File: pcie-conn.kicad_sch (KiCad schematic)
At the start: 22 parts, among them J2 Bus_M.2_1-2199230-6

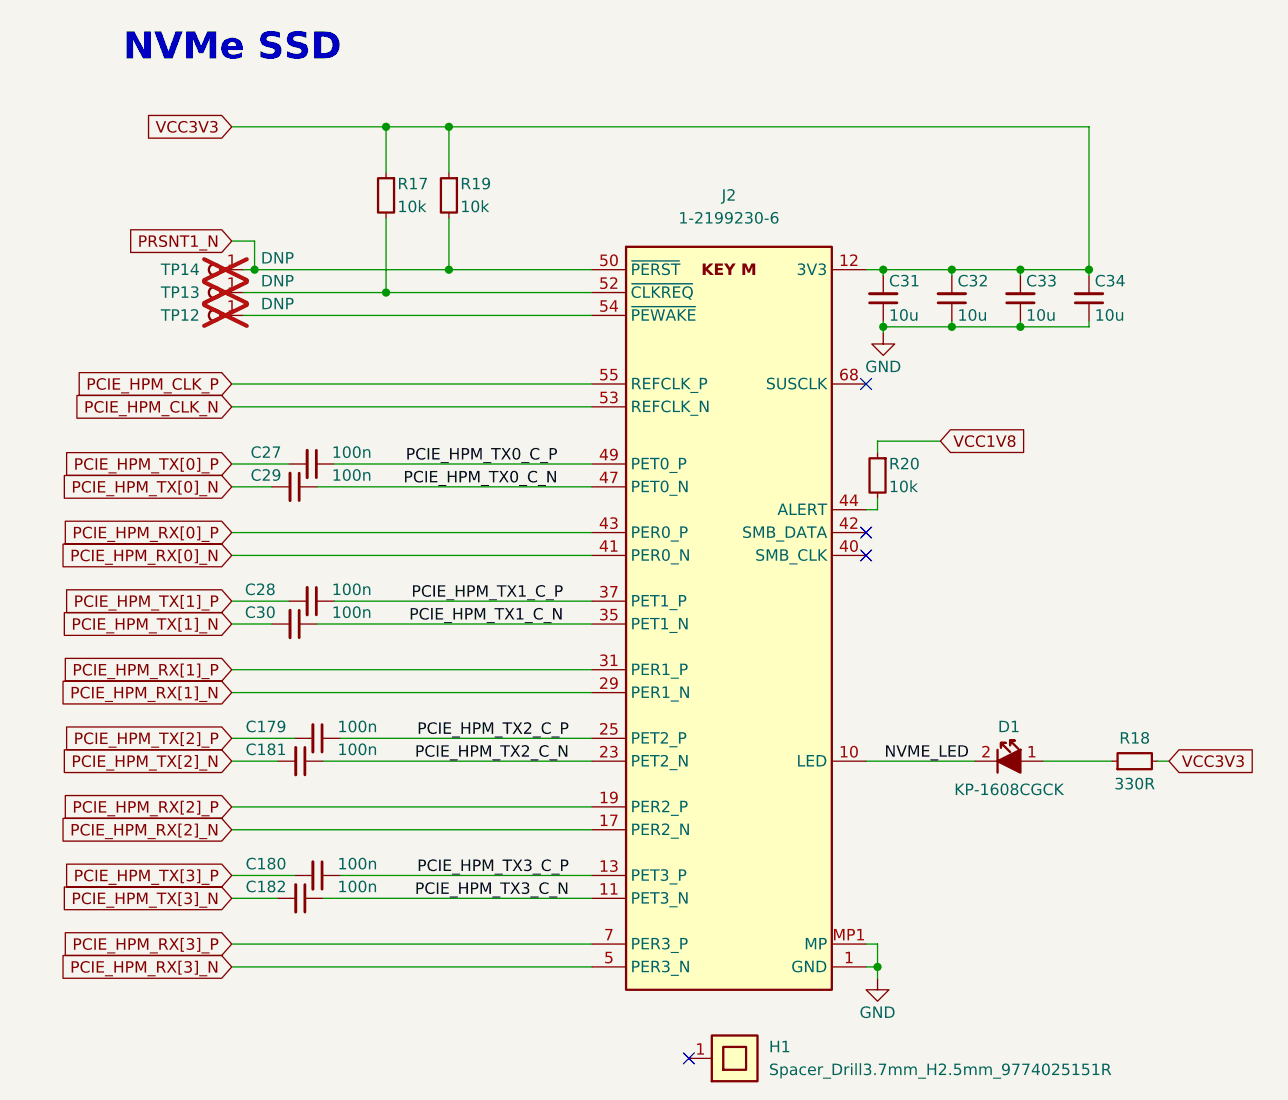
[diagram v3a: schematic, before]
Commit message: [#68236] Allign sch to grid
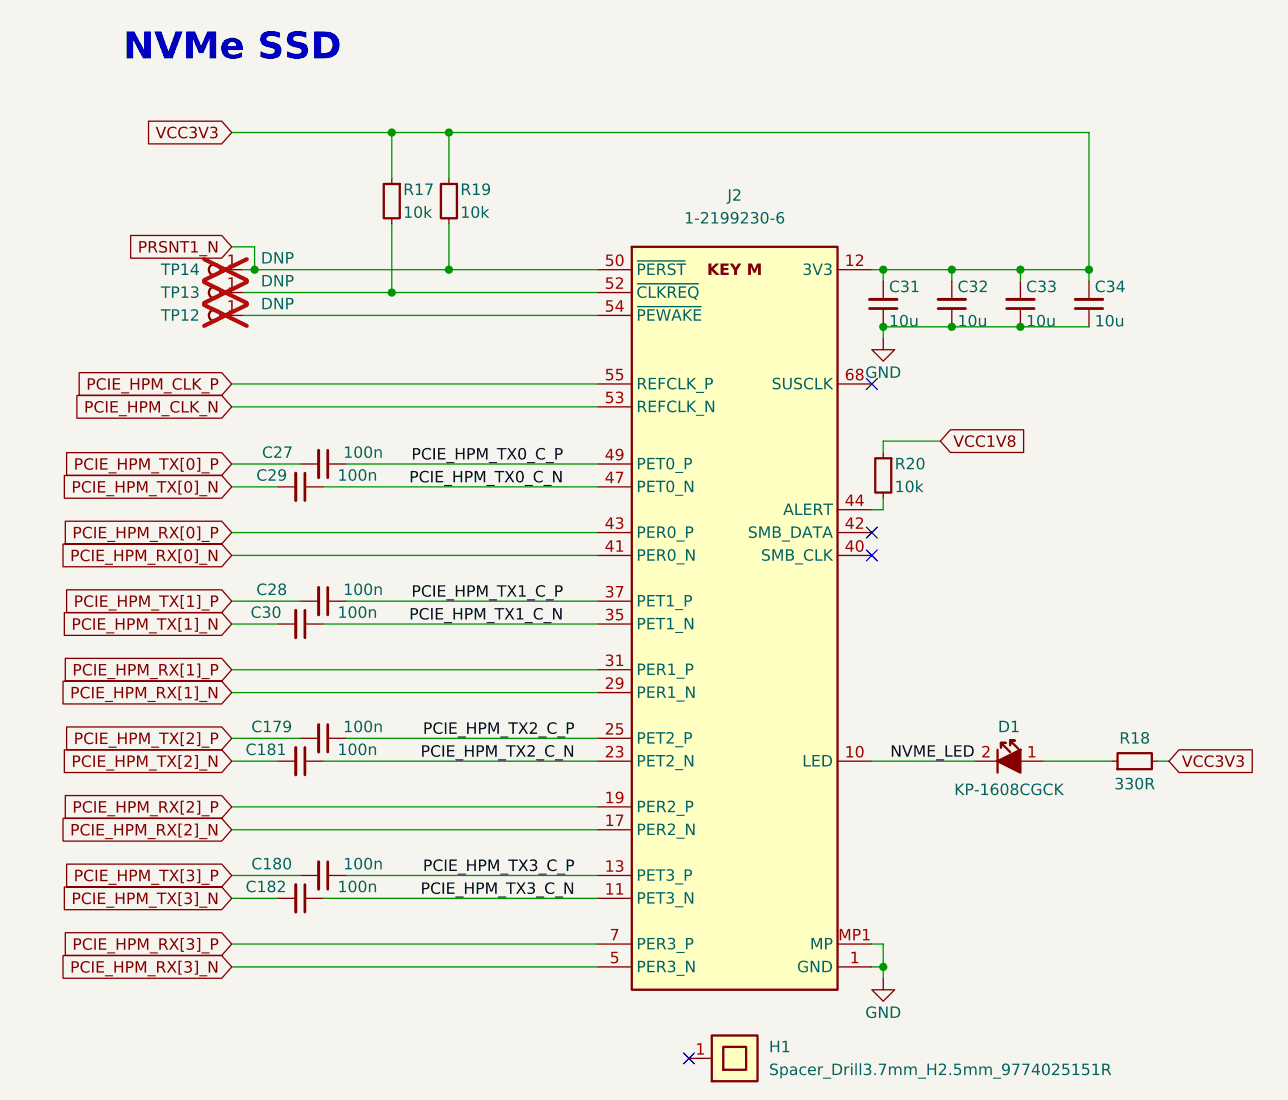
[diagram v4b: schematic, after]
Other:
- moved on the sheet: C179, C180, C27, C28, C29, C30, C31, C32, C33, C34, J2, R17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

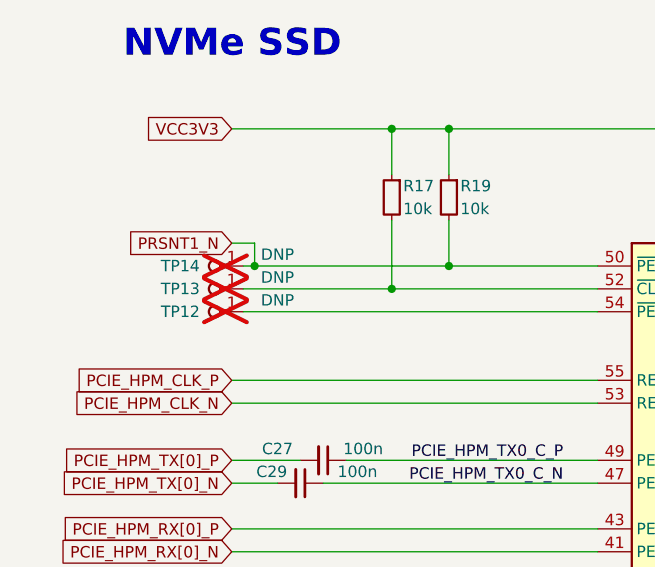
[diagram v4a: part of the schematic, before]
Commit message: [#68236] Remove DNP property from Testpoints
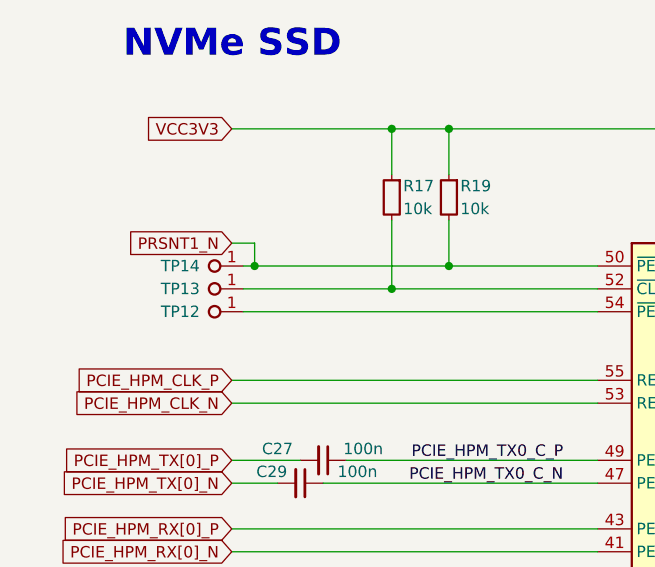
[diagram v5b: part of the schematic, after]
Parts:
- TP12, TP13, TP14: DNP DNP -> (none); now fitted
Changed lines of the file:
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@@
   )
   (symbol (lib_id "antmicroTestPoints:TP_1mm_SMD") (at 175.26 102.87 180) (unit 1)
-    (in_bom no) (on_board yes) (dnp yes)
+    (in_bom no) (on_board yes) (dnp no)
     (property "Reference" "TP12" (at 168.275 102.87 0)
       (effects (font (size 1.27 1.27)))
@@
       (effects (font (size 1.27 1.27) (thickness 0.15)) (justify left bottom) hide)
     )
-    (property "DNP" "DNP" (at 179.07 101.6 0)
-      (effects (font (size 1.27 1.27)))
-    )
     (pin "1")
     (instances
@@
   )
   (symbol (lib_id "antmicroTestPoints:TP_1mm_SMD") (at 175.26 100.33 180) (unit 1)
-    (in_bom no) (on_board yes) (dnp yes)
+    (in_bom no) (on_board yes) (dnp no)
     (property "Reference" "TP13" (at 168.275 100.33 0)
       (effects (font (size 1.27 1.27)))
@@
       (effects (font (size 1.27 1.27) (thickness 0.15)) (justify left bottom) hide)
     )
-    (property "DNP" "DNP" (at 179.07 99.06 0)
-      (effects (font (size 1.27 1.27)))
-    )
     (pin "1")
     (instances
@@
   )
   (symbol (lib_id "antmicroTestPoints:TP_1mm_SMD") (at 175.26 97.79 0) (mirror y) (unit 1)
-    (in_bom no) (on_board yes) (dnp yes)
+    (in_bom no) (on_board yes) (dnp no)
     (property "Reference" "TP14" (at 168.275 97.79 0)
       (effects (font (size 1.27 1.27)))
@@
       (effects (font (size 1.27 1.27) (thickness 0.15)) (justify left bottom) hide)
     )
-    (property "DNP" "DNP" (at 179.07 96.52 0)
-      (effects (font (size 1.27 1.27)))
-    )
     (pin "1")
